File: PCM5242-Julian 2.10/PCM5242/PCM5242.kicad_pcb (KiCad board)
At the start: 2 copper layers, 37 parts, among them IC1 NCP163ASN330T1G, IC2 NCP163ASN330T1G, J1 Conn_01x10_Male, J2 Conn_01x10_Male, J3 Conn_01x03_Male, U1 PCM5242, Y1 ASE-24.000MHZ-ET

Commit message: Add files via upload
Some progress was made on the PCB and schematic should be finished. Everything is placed, now I need to route and make the ground pours.
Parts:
- removed C3: 0.1uF, Capacitor_SMD:C_0603_1608Metric_Pad1.08x0.95mm_HandSolder
- removed R1: 10k, Resistor_SMD:R_1206_3216Metric_Pad1.30x1.75mm_HandSolder
- C4: value 2.2uF -> 0.1uF
- J1: value Conn_01x10_Male -> Conn_01x04_Male; footprint Connector_PinHeader_2.54mm:PinHeader_1x10_P2.54mm_Vertical -> Connector_PinHeader_2.54mm:PinHeader_1x04_P2.54mm_Vertical
- J2: value Conn_01x10_Male -> Conn_01x12_Male; footprint Connector_PinHeader_2.54mm:PinHeader_1x10_P2.54mm_Vertical -> Connector_PinHeader_2.54mm:PinHeader_1x12_P2.54mm_Vertical
- moved R10 102.5 mm to (80.4, 117.8), turned to 90 degrees
- moved R9 98.7 mm to (89.7, 116.0), turned to -90 degrees
- moved C12 96.9 mm to (80.2, 110.3), turned to 180 degrees
- moved C11 91.4 mm to (88.4, 111.3), turned to 180 degrees
- moved R11 87.7 mm to (94.8, 120.8), turned to 90 degrees
- moved C13 87.1 mm to (55.6, 110.8)
- moved R7 85.7 mm to (94.8, 115.5), turned to -90 degrees
- moved R2 84.9 mm to (89.7, 107.1), turned to -90 degrees
- moved R4 84.9 mm to (80.4, 106.9), turned to -90 degrees
- moved C9 82.6 mm to (89.1, 100.3), turned to -90 degrees
- moved C15 81.7 mm to (55.5, 106.8)
- moved R5 81.6 mm to (86.8, 107.0), turned to -90 degrees
- moved C4 78.2 mm to (80.4, 96.1)
- moved C10 75.7 mm to (86.4, 100.3), turned to -90 degrees
- moved R8 75.2 mm to (76.7, 112.8), turned to -90 degrees
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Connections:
- C1 pad 1: VCC -> AVDD
- C4 pad 1: VCC -> AVDD
- J1 pad 1: GNDD -> /A1
- J1 pad 2: GNDD -> /A2
- J1 pad 3: /A2 -> /A3
- J1 pad 4: /A3 -> /A4
- J2 pad 1: XSMT -> GNDD
- J2 pad 10: unconnected-(J2-Pad10) -> /A13
- J2 pad 2: /A10 -> /A5
- J2 pad 3: /A11 -> /A6
- J2 pad 4: /A12 -> /A7
- J2 pad 5: /A13 -> /A8
- J2 pad 6: /A14 -> /A9
- J2 pad 7: /A15 -> /A10
- J2 pad 8: /A16 -> /A11
- J2 pad 9: /A17 -> /A12
- R10 pad 1: GNDD -> /A1
- R11 pad 1: GNDD -> /A4
- R11 pad 2: /A4 -> Net-(R11-Pad2)
- R7 pad 2: /A4 -> Net-(R11-Pad2)
- U1 pad 1: XSMT -> AVDD
- U1 pad 23: /A11 -> GNDD
- U1 pad 24: /A12 -> DVDD
- U1 pad 25: /A13 -> /A11
- U1 pad 27: /A14 -> /A12
- U1 pad 28: /A15 -> /A13
- U1 pad 29: unconnected-(U1-Pad29) -> /No Connect
- U1 pad 30: unconnected-(U1-Pad30) -> /No Connect
- U1 pad 31: /A16 -> /A14
- U1 pad 32: /A17 -> /A15
- U1 pad 5: VCC -> AVDD
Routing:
- net /A15: track 0.00 -> 39.4 mm
- net /A14: track 0.00 -> 37.8 mm
- net /A13: track 0.00 -> 35.4 mm
- net /A12: track 0.00 -> 33.7 mm
- net /A11: track 0.00 -> 31.2 mm
- net /A10: track 0.00 -> 30.1 mm
- net /A9: track 0.00 -> 29.3 mm
- net /A8: track 0.00 -> 28.4 mm
- net /A7: track 0.00 -> 27.6 mm
- net /A6: track 0.00 -> 26.7 mm
- net /A5: track 0.00 -> 25.9 mm
- net Net-(R5-Pad1): track 0.00 -> 9.65 mm
- net Net-(R2-Pad1): track 0.00 -> 9.54 mm
- net Net-(C11-Pad1): track 0.00 -> 9.47 mm
- net Net-(R4-Pad1): track 0.00 -> 9.05 mm
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
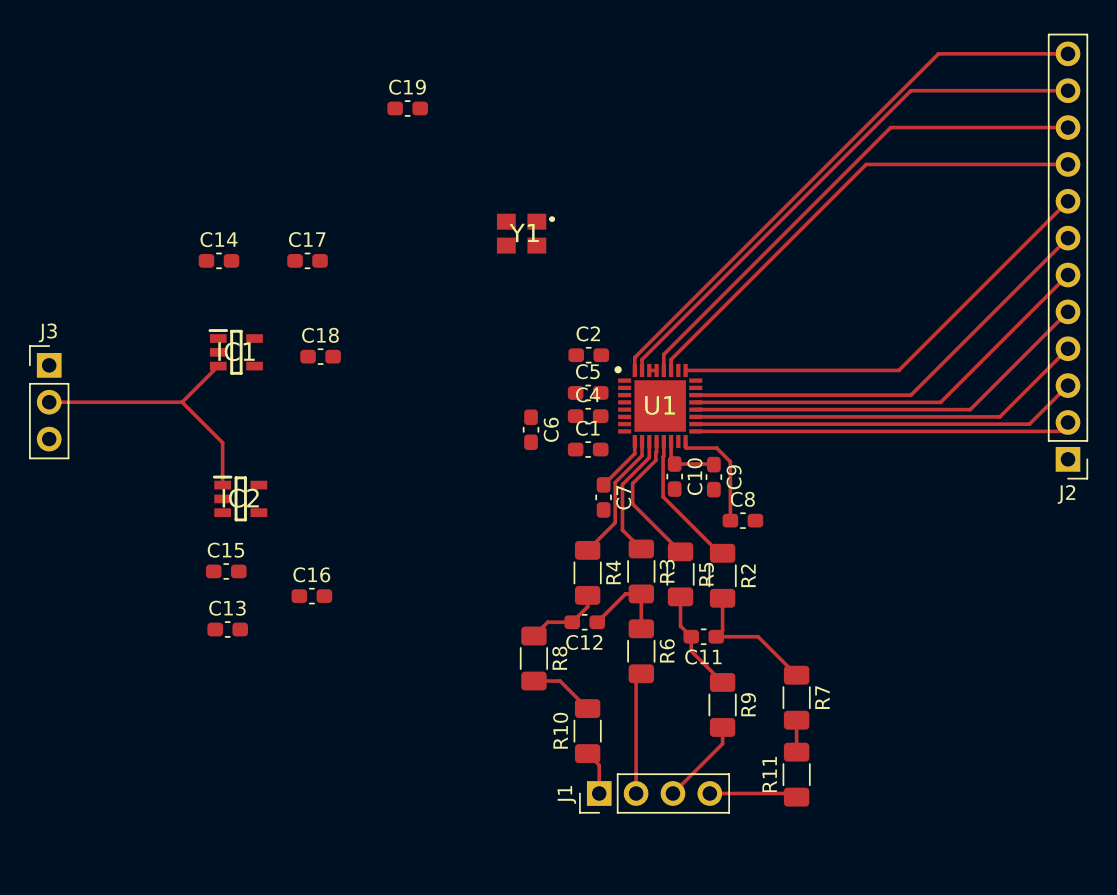
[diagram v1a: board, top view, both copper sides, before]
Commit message: Updated PCB
Almost finished routing and pouring, I have some design questions for tomorrow.
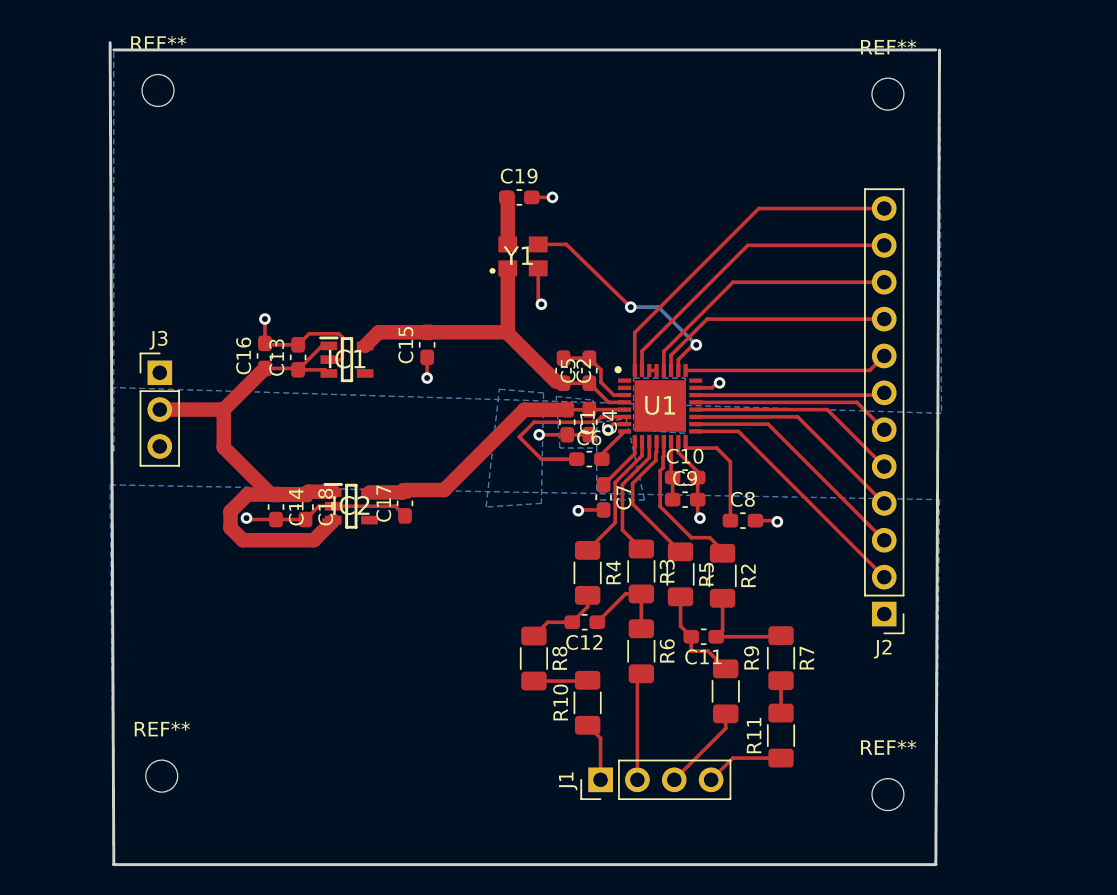
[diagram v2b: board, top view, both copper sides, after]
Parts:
- added REF**: MountingHole_2.2mm_M2, MountingHole:MountingHole_2.2mm_M2, F.Cu at (101.1, 73.9)
- added REF**: MountingHole_2.2mm_M2, MountingHole:MountingHole_2.2mm_M2, F.Cu at (101.1, 122.2)
- added REF**: MountingHole_2.2mm_M2, MountingHole:MountingHole_2.2mm_M2, F.Cu at (50.8, 73.7)
- added REF**: MountingHole_2.2mm_M2, MountingHole:MountingHole_2.2mm_M2, F.Cu at (51.1, 120.9)
- moved C15 20.9 mm to (69.3, 91.2), turned to 90 degrees
- moved C13 19.4 mm to (60.5, 92.0), turned to 90 degrees
- moved C17 18.0 mm to (67.8, 102.1), turned to 90 degrees
- moved C14 17.4 mm to (58.9, 102.4), turned to -90 degrees
- moved C16 16.9 mm to (58.2, 91.9), turned to 90 degrees
- moved J2 16.6 mm to (100.8, 109.7)
- moved C18 10.4 mm to (61.0, 102.4), turned to -90 degrees
- moved C19 9.83 mm to (75.7, 81.0)
- moved IC2 7.64 mm to (64.1, 102.3)
- moved J3 7.64 mm to (50.9, 93.1)
- moved IC1 7.64 mm to (63.8, 92.2)
- moved C6 4.50 mm to (80.5, 99.1), turned to 0 degrees
- moved R7 2.93 mm to (93.7, 112.8)
- moved R11 2.90 mm to (93.7, 118.1)
- moved C9 2.52 mm to (87.1, 101.9), turned to 0 degrees
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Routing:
- net DVDD: track 0.00 -> 27.4 mm
- net GNDD: track 0.00 -> 26.8 mm, vias 0 -> 6
- net VCC: track 19.7 -> 43.7 mm
- net GNDA: track 0.00 -> 22.2 mm, vias 0 -> 5
- net AVDD: track 4.64 -> 24.1 mm
- net /A11: track 31.2 -> 14.1 mm
- net /A10: track 30.1 -> 13.1 mm
- net /A13: track 35.4 -> 18.5 mm
- net /A12: track 33.7 -> 16.8 mm
- net SCK: track 0.00 -> 16.2 mm, vias 0 -> 2
- net /A14: track 37.8 -> 21.6 mm
- net /A15: track 39.4 -> 23.3 mm
- net /A9: track 29.3 -> 13.8 mm
- net /A8: track 28.4 -> 14.6 mm
- net Net-(C6-Pad1): track 0.00 -> 12.4 mm
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- added copper zone on B.Cu, net (none)
- added copper zone on B.Cu, net DVDD
- added copper zone on B.Cu, net GNDA
- added copper zone on B.Cu, net GNDD
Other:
- board outline added: 57.1 x 56.6 mm
